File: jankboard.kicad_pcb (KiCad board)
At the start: 2 copper layers, 145.3 x 81 mm, 159 parts, among them J1 F31L-1A7H1-11030, J2 F31L-1A7H1-11030, J3 Conn_01x02, J4 Conn_01x02, J5 Conn_01x04_Pin, SW1 SW_Push_45deg, SW10 SW_Push_45deg, SW11 SW_Push_45deg, SW12 SW_Push_45deg, SW13 SW_Push_45deg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

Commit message: add models
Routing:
- net +3.3V: track 103.6 -> 95.9 mm
- net SCK: track 34.8 -> 36.1 mm
- net CS: track 37.5 -> 38.4 mm
- net DC: track 38.9 -> 39.6 mm
- net BUSY: track 38.8 -> 39.4 mm

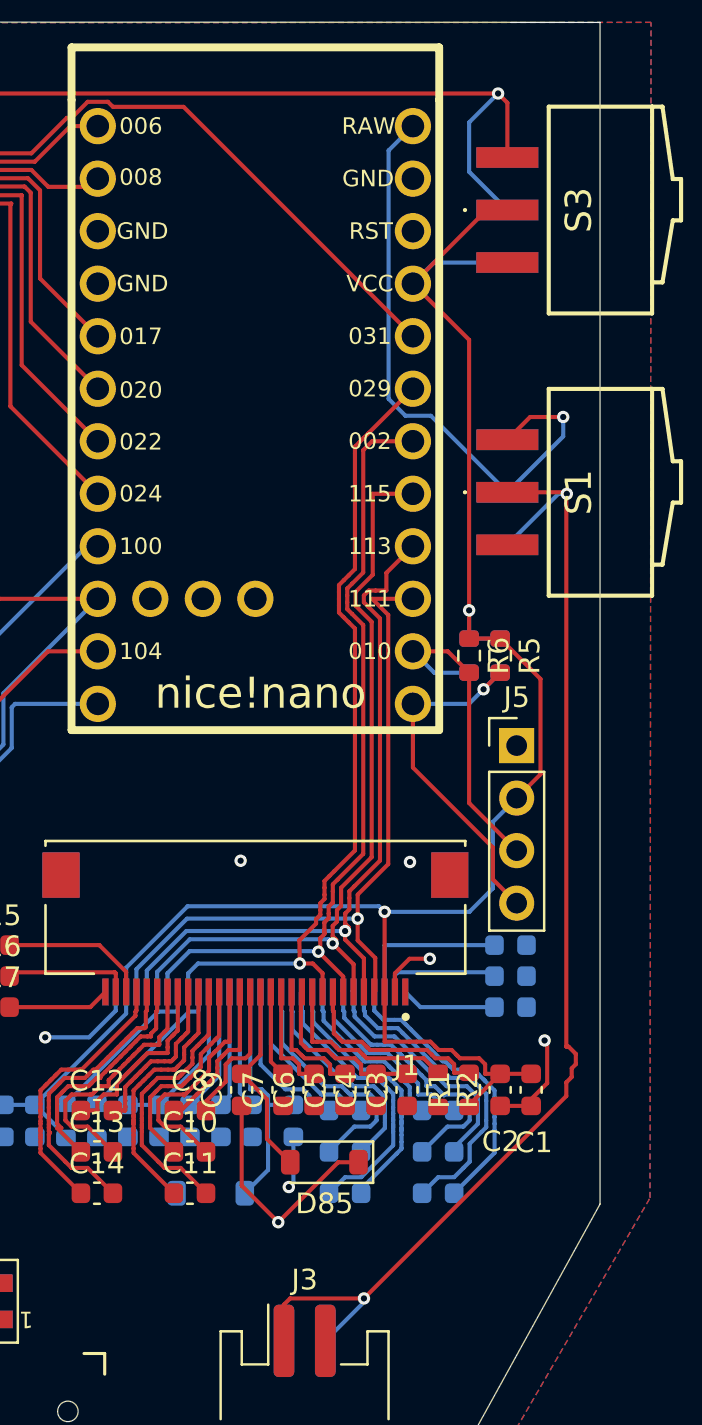
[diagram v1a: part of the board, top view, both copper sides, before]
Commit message: make room for hole
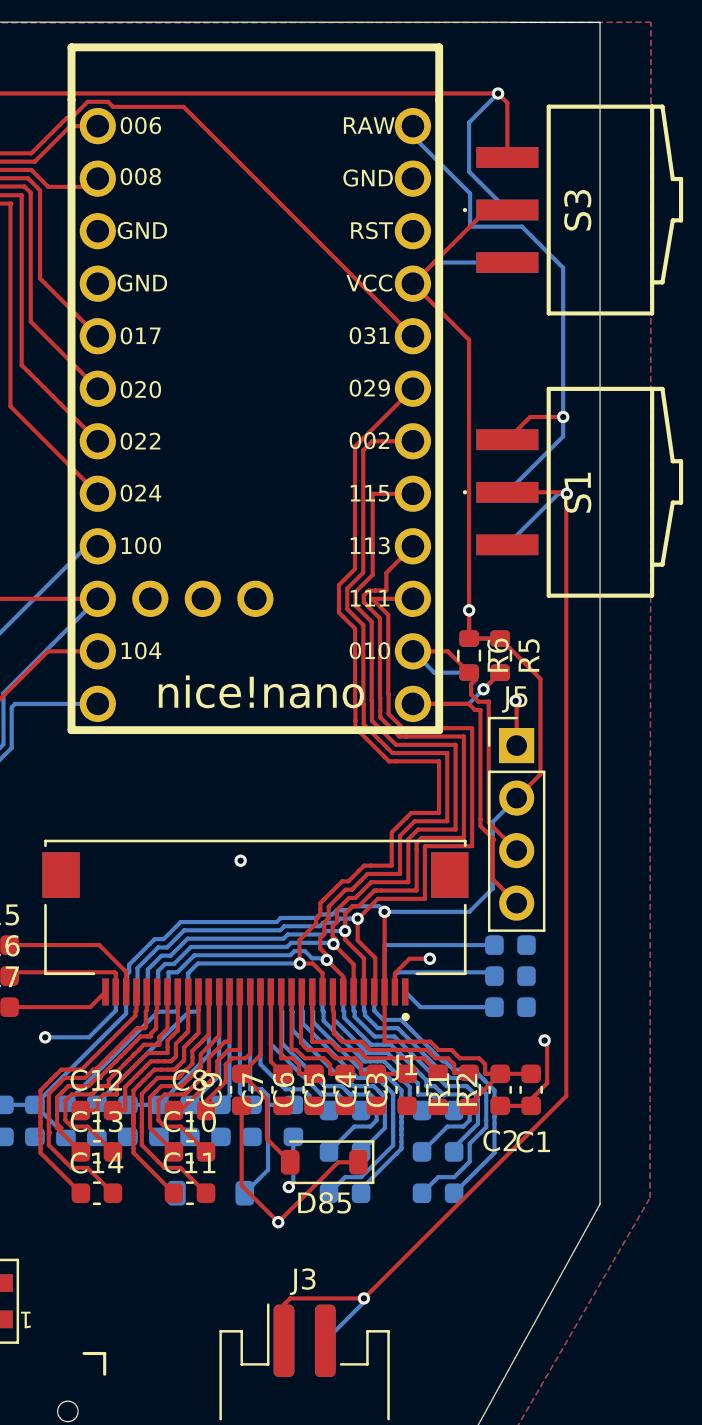
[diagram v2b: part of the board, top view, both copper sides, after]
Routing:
- net DIN: track 35.1 -> 43.1 mm
- net SCK: track 36.1 -> 43.7 mm
- net DC: track 39.6 -> 47.0 mm
- net CS: track 38.4 -> 45.7 mm
- net BUSY: track 39.4 -> 45.9 mm
- net Net-(S1-NO): track 29.2 -> 26.5 mm
- net GND: track 76.9 -> 79.1 mm
- net SDA: track 17.7 -> 19.5 mm

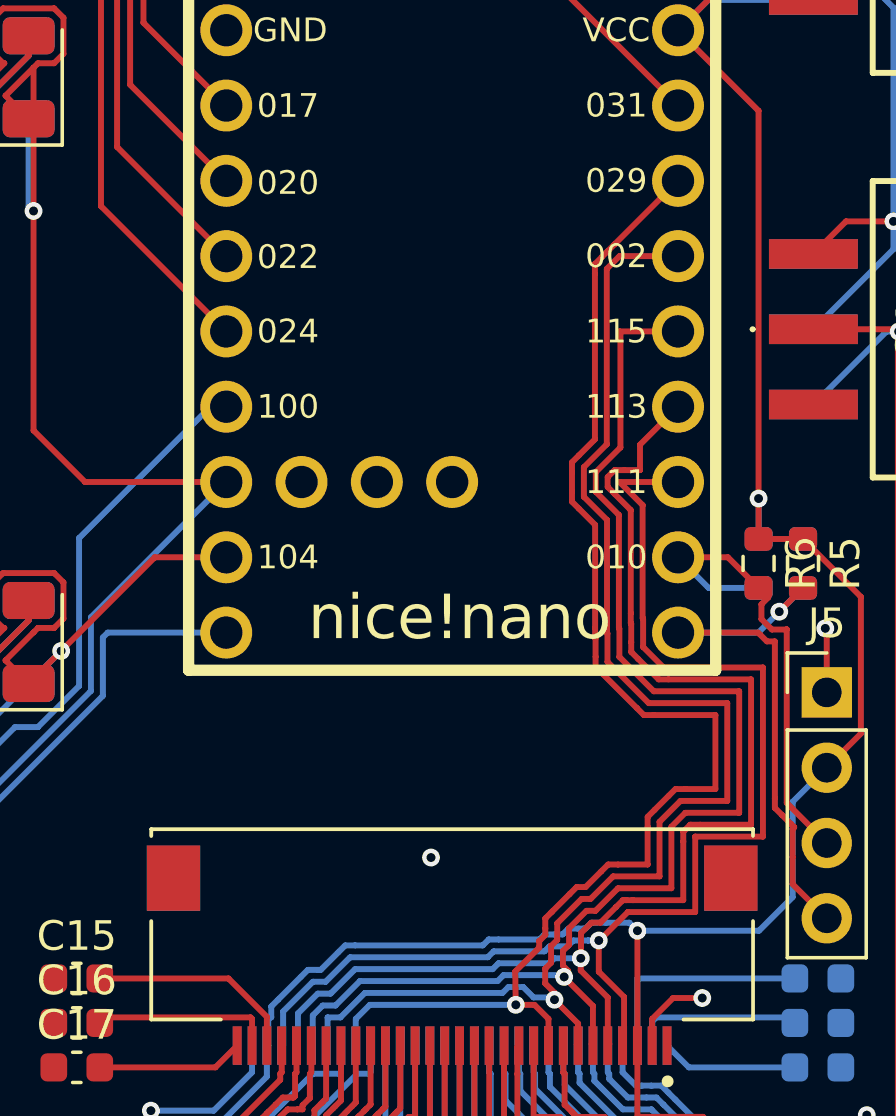
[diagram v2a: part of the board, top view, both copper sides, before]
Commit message: add hole
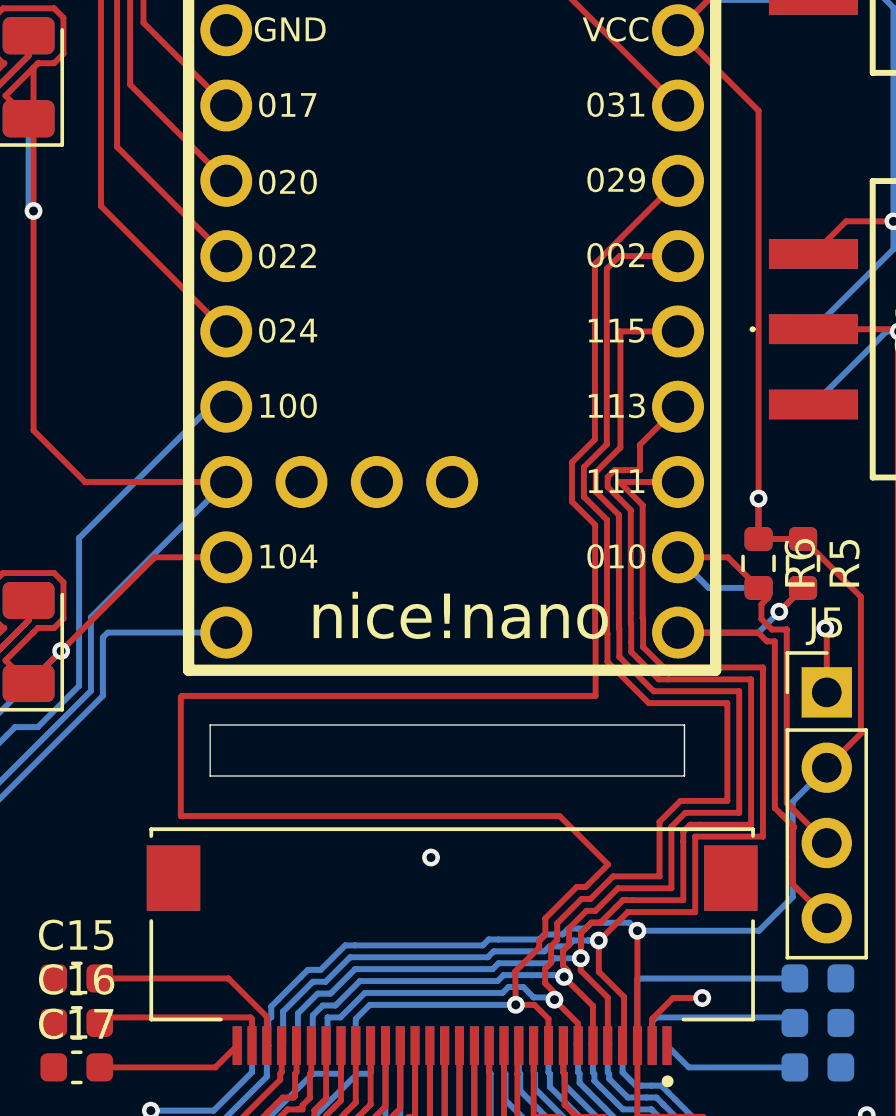
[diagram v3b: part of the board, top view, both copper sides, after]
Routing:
- net BUSY: track 45.9 -> 67.2 mm
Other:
- outline, holes or cut-outs redrawn
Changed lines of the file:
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@@
 		)
 	)
+	(gr_rect
+		(start 149 59.95)
+		(end 165 61.67)
+		(stroke
+			(width 0.05)
+			(type solid)
+		)
+		(fill no)
+		(layer "Edge.Cuts")
+	)
 	(gr_line
 		(start 28.575 85.725)
@@
 	)
 	(segment
-		(start 163.395546 59.3789)
-		(end 162.2361 58.219454)
+		(start 161.2056 52.4169)
+		(end 161.2056 51.0881)
 		(width 0.2)
 		(layer "F.Cu")
@@
 	)
 	(segment
-		(start 160.306 66.804957)
+		(start 160.306 67.032098)
 		(end 160.306 66.472757)
 		(width 0.2)
@@
 	)
 	(segment
-		(start 160.099241 67.238857)
-		(end 160.306 67.032098)
-		(width 0.2)
-		(layer "F.Cu")
-		(net 131)
-	)
-	(segment
-		(start 163.7575 63.3818)
-		(end 163.7575 63.0496)
-		(width 0.2)
-		(layer "F.Cu")
-		(net 131)
-	)
-	(segment
-		(start 162.0012 57.984554)
-		(end 162.0012 57.652354)
+		(start 148.01 63.02)
+		(end 148.01 59.005478)
 		(width 0.2)
 		(layer "F.Cu")
@@
 	(segment
 		(start 160.306 66.472757)
-		(end 160.506 66.272757)
+		(end 161.362757 65.416)
 		(width 0.2)
 		(layer "F.Cu")
@@
 	)
 	(segment
-		(start 161.2056 52.0847)
-		(end 161.2056 51.4203)
+		(start 160.7896 63.02)
+		(end 148.01 63.02)
 		(width 0.2)
 		(layer "F.Cu")
@@
 	)
 	(segment
-		(start 166.044 62.11)
-		(end 166.044 59.6138)
-		(width 0.2)
-		(layer "F.Cu")
-		(net 131)
-	)
-	(segment
-		(start 163.7575 63.0496)
-		(end 163.9924 62.8147)
-		(width 0.2)
-		(layer "F.Cu")
-		(net 131)
-	)
-	(segment
-		(start 162.4086 43.9664)
-		(end 162.6435 43.7315)
+		(start 161.362757 65.416)
+		(end 161.6656 65.416)
 		(width 0.2)
 		(layer "F.Cu")
@@
 	)
 	(segment
-		(start 160.506 66.272757)
-		(end 160.5409 66.237857)
+		(start 161.986 57.0144)
+		(end 161.986 53.1973)
 		(width 0.2)
 		(layer "F.Cu")
@@
 	)
 	(segment
-		(start 163.962646 59.6138)
-		(end 163.630446 59.6138)
-		(width 0.2)
-		(layer "F.Cu")
-		(net 131)
-	)
-	(segment
-		(start 162.2139 44.1611)
-		(end 162.4086 43.9664)
-		(width 0.2)
-		(layer "F.Cu")
-		(net 131)
-	)
-	(segment
-		(start 161.4405 50.8532)
-		(end 161.979 50.3147)
-		(width 0.2)
-		(layer "F.Cu")
-		(net 131)
-	)
-	(segment
-		(start 161.127857 65.6509)
-		(end 161.362757 65.416)
-		(width 0.2)
-		(layer "F.Cu")
-		(net 131)
-	)
-	(segment
-		(start 165.0293 62.11)
-		(end 166.044 62.11)
+		(start 161.979 50.3147)
+		(end 161.979 44.396)
 		(width 0.2)
 		(layer "F.Cu")
@@
 	(segment
 		(start 162.4256 64.656)
-		(end 162.7578 64.656)
-		(width 0.2)
-		(layer "F.Cu")
-		(net 131)
-	)
-	(segment
-		(start 162.0012 57.652354)
-		(end 162.0012 57.0296)
-		(width 0.2)
-		(layer "F.Cu")
-		(net 131)
-	)
-	(segment
-		(start 164.6971 62.11)
-		(end 165.0293 62.11)
+		(end 160.7896 63.02)
 		(width 0.2)
 		(layer "F.Cu")
@@
 	(segment
 		(start 161.986 53.1973)
-		(end 161.4405 52.6518)
-		(width 0.2)
-		(layer "F.Cu")
-		(net 131)
-	)
-	(segment
-		(start 162.6435 43.7315)
-		(end 164.7825 41.5925)
-		(width 0.2)
-		(layer "F.Cu")
-		(net 131)
-	)
-	(segment
-		(start 161.4405 52.6518)
 		(end 161.2056 52.4169)
 		(width 0.2)
@@
 	)
 	(segment
-		(start 161.362757 65.416)
-		(end 161.6656 65.416)
-		(width 0.2)
-		(layer "F.Cu")
-		(net 131)
-	)
-	(segment
-		(start 163.9924 62.8147)
-		(end 164.4622 62.3449)
-		(width 0.2)
-		(layer "F.Cu")
-		(net 131)
-	)
-	(segment
-		(start 163.7575 64.656)
-		(end 163.7575 63.3818)
-		(width 0.2)
-		(layer "F.Cu")
-		(net 131)
-	)
-	(segment
-		(start 161.2056 52.4169)
-		(end 161.2056 52.0847)
-		(width 0.2)
-		(layer "F.Cu")
-		(net 131)
-	)
-	(segment
-		(start 159.31 69.39)
-		(end 159.29 68.2675)
-		(width 0.2)
-		(layer "F.Cu")
-		(net 131)
-	)
-	(segment
-		(start 161.986 57.0144)
-		(end 161.986 56.6822)
-		(width 0.2)
-		(layer "F.Cu")
-		(net 131)
-	)
-	(segment
-		(start 161.986 56.6822)
-		(end 161.986 53.1973)
-		(width 0.2)
-		(layer "F.Cu")
-		(net 131)
-	)
-	(segment
-		(start 161.979 44.7282)
-		(end 161.979 44.396)
-		(width 0.2)
-		(layer "F.Cu")
-		(net 131)
-	)
-	(segment
-		(start 160.5409 66.237857)
-		(end 161.127857 65.6509)
-		(width 0.2)
-		(layer "F.Cu")
-		(net 131)
-	)
-	(segment
-		(start 164.4622 62.3449)
-		(end 164.6971 62.11)
-		(width 0.2)
-		(layer "F.Cu")
-		(net 131)
-	)
-	(segment
-		(start 162.7578 64.656)
-		(end 163.7575 64.656)
+		(start 162.0012 58.97)
+		(end 162.0012 57.0296)
 		(width 0.2)
 		(layer "F.Cu")
@@
 	)
 	(segment
-		(start 162.1907 64.8909)
-		(end 162.4256 64.656)
+		(start 148.01 59.005478)
+		(end 148.045478 58.97)
 		(width 0.2)
 		(layer "F.Cu")
@@
 	)
 	(segment
-		(start 166.044 59.6138)
-		(end 163.962646 59.6138)
+		(start 148.045478 58.97)
+		(end 162.0012 58.97)
 		(width 0.2)
 		(layer "F.Cu")
@@
 	(segment
 		(start 161.6656 65.416)
-		(end 162.1907 64.8909)
+		(end 162.4256 64.656)
 		(width 0.2)
 		(layer "F.Cu")
@@
 	)
 	(segment
-		(start 161.979 44.396)
-		(end 162.2139 44.1611)
+		(start 160.099241 67.238857)
+		(end 160.306 67.032098)
 		(width 0.2)
 		(layer "F.Cu")
@@
 	(segment
 		(start 161.2056 51.0881)
-		(end 161.4405 50.8532)
-		(width 0.2)
-		(layer "F.Cu")
-		(net 131)
-	)
-	(segment
-		(start 161.2056 51.4203)
-		(end 161.2056 51.0881)
-		(width 0.2)
-		(layer "F.Cu")
-		(net 131)
-	)
-	(segment
-		(start 163.630446 59.6138)
-		(end 163.395546 59.3789)
-		(width 0.2)
-		(layer "F.Cu")
-		(net 131)
-	)
-	(segment
-		(start 161.979 50.3147)
-		(end 161.979 44.7282)
+		(end 161.979 50.3147)
 		(width 0.2)
 		(layer "F.Cu")
@@
 	)
 	(segment
-		(start 162.2361 58.219454)
-		(end 162.0012 57.984554)
+		(start 161.979 44.396)
+		(end 164.7825 41.5925)
 		(width 0.2)
 		(layer "F.Cu")
@@
 	)
 	(segment
-		(start 160.306 67.032098)
-		(end 160.306 66.804957)
+		(start 159.31 69.39)
+		(end 159.29 68.2675)
 		(width 0.2)
 		(layer "F.Cu")

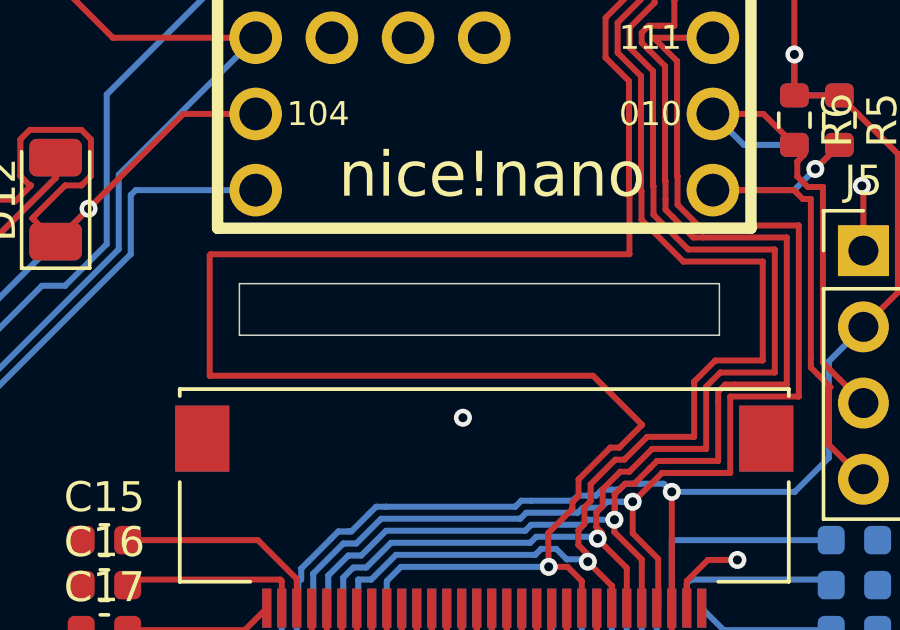
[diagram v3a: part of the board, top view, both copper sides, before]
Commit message: elongate holes slightly for better clearance of fpc cable
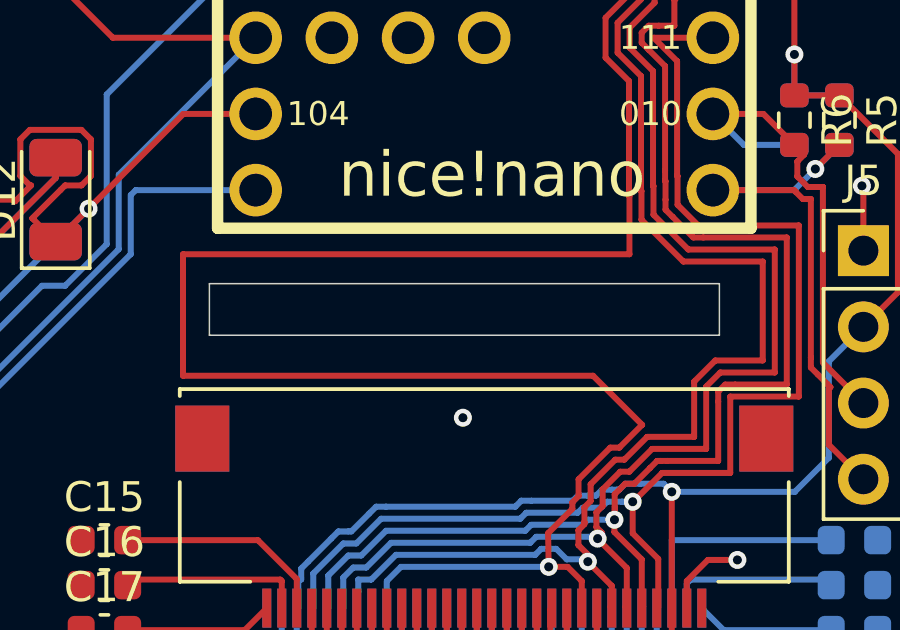
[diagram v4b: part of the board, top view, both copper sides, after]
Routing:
- net BUSY: track 67.2 -> 69.0 mm
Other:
- outline, holes or cut-outs redrawn
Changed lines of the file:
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@@
 	)
 	(gr_rect
-		(start 149 59.95)
+		(start 148 59.95)
 		(end 165 61.67)
 		(stroke
@@
 	)
 	(segment
-		(start 161.2056 52.4169)
-		(end 161.2056 51.0881)
-		(width 0.2)
-		(layer "F.Cu")
-		(net 131)
-	)
-	(segment
-		(start 160.306 67.032098)
-		(end 160.306 66.472757)
+		(start 161.6656 65.416)
+		(end 162.4256 64.656)
 		(width 0.2)
 		(layer "F.Cu")
@@
 	)
 	(segment
-		(start 148.01 63.02)
-		(end 148.01 59.005478)
+		(start 161.986 57.0144)
+		(end 161.986 53.1973)
 		(width 0.2)
 		(layer "F.Cu")
@@
 	)
 	(segment
-		(start 160.306 66.472757)
-		(end 161.362757 65.416)
+		(start 160.4125 69.863)
+		(end 159.9395 69.39)
 		(width 0.2)
 		(layer "F.Cu")
@@
 	)
 	(segment
-		(start 160.4125 69.863)
-		(end 159.9395 69.39)
+		(start 147.12 58.97)
+		(end 162.0012 58.97)
 		(width 0.2)
 		(layer "F.Cu")
@@
 	)
 	(segment
-		(start 160.7896 63.02)
-		(end 148.01 63.02)
+		(start 161.979 44.396)
+		(end 164.7825 41.5925)
 		(width 0.2)
 		(layer "F.Cu")
@@
 	)
 	(segment
-		(start 161.362757 65.416)
-		(end 161.6656 65.416)
+		(start 160.306 66.472757)
+		(end 161.362757 65.416)
 		(width 0.2)
 		(layer "F.Cu")
@@
 	)
 	(segment
-		(start 161.986 57.0144)
-		(end 161.986 53.1973)
+		(start 162.0012 58.97)
+		(end 162.0012 57.0296)
 		(width 0.2)
 		(layer "F.Cu")
@@
 	)
 	(segment
-		(start 160.099241 67.458259)
-		(end 160.099241 67.238857)
+		(start 159.29 68.2675)
+		(end 160.099241 67.458259)
 		(width 0.2)
 		(layer "F.Cu")
@@
 	)
 	(segment
-		(start 162.0012 57.0296)
-		(end 161.986 57.0144)
+		(start 161.2056 52.4169)
+		(end 161.2056 51.0881)
 		(width 0.2)
 		(layer "F.Cu")
@@
 	)
 	(segment
-		(start 162.4256 64.656)
-		(end 160.7896 63.02)
+		(start 160.306 67.032098)
+		(end 160.306 66.472757)
 		(width 0.2)
 		(layer "F.Cu")
@@
 	)
 	(segment
-		(start 161.986 53.1973)
-		(end 161.2056 52.4169)
+		(start 159.31 69.39)
+		(end 159.29 68.2675)
 		(width 0.2)
 		(layer "F.Cu")
@@
 	)
 	(segment
-		(start 162.0012 58.97)
-		(end 162.0012 57.0296)
+		(start 162.4256 64.656)
+		(end 160.7896 63.02)
 		(width 0.2)
 		(layer "F.Cu")
@@
 	)
 	(segment
-		(start 148.01 59.005478)
-		(end 148.045478 58.97)
+		(start 160.099241 67.238857)
+		(end 160.306 67.032098)
 		(width 0.2)
 		(layer "F.Cu")
@@
 	)
 	(segment
-		(start 148.045478 58.97)
-		(end 162.0012 58.97)
+		(start 160.7896 63.02)
+		(end 147.12 63.02)
 		(width 0.2)
 		(layer "F.Cu")
@@
 	)
 	(segment
-		(start 161.6656 65.416)
-		(end 162.4256 64.656)
+		(start 162.0012 57.0296)
+		(end 161.986 57.0144)
 		(width 0.2)
 		(layer "F.Cu")
@@
 	)
 	(segment
-		(start 159.29 68.2675)
-		(end 160.099241 67.458259)
+		(start 161.362757 65.416)
+		(end 161.6656 65.416)
 		(width 0.2)
 		(layer "F.Cu")
@@
 	)
 	(segment
-		(start 160.099241 67.238857)
-		(end 160.306 67.032098)
+		(start 159.9395 69.39)
+		(end 159.31 69.39)
 		(width 0.2)
 		(layer "F.Cu")
@@
 	)
 	(segment
-		(start 159.9395 69.39)
-		(end 159.31 69.39)
+		(start 160.4125 70.765)
+		(end 160.4125 69.863)
 		(width 0.2)
 		(layer "F.Cu")
@@
 	)
 	(segment
-		(start 160.4125 70.765)
-		(end 160.4125 69.863)
+		(start 161.986 53.1973)
+		(end 161.2056 52.4169)
 		(width 0.2)
 		(layer "F.Cu")
@@
 	)
 	(segment
-		(start 161.2056 51.0881)
-		(end 161.979 50.3147)
+		(start 160.099241 67.458259)
+		(end 160.099241 67.238857)
 		(width 0.2)
 		(layer "F.Cu")
@@
 	)
 	(segment
-		(start 161.979 44.396)
-		(end 164.7825 41.5925)
+		(start 161.2056 51.0881)
+		(end 161.979 50.3147)
 		(width 0.2)
 		(layer "F.Cu")
@@
 	)
 	(segment
-		(start 159.31 69.39)
-		(end 159.29 68.2675)
+		(start 147.12 63.02)
+		(end 147.12 58.97)
 		(width 0.2)
 		(layer "F.Cu")
